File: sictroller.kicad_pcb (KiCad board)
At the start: 6 copper layers, 135.8 x 121.3 mm, 314 parts, among them J1 CONN_01X02, J10 CONN_01X02, J11 RINGTERM, J12 RINGTERM, J14 CONN_01X05, J15 CONN_01X03, J2 CONN_01X08, J3 CONN_02X05, J4 RINGTERM, J5 RINGTERM, J6 RINGTERM, J7 CONN_01X02, J8 RINGTERM, J9 RINGTERM, Q1 CSD17483F4, Q2 CCS050M12CM2, T1 7508110151, U1 ACPL-M61L, U10 74LVC2G04, U11 TXS0108E, U12 MGJ1, U13 MGJ1, U14 2ED020I12-F2, U15 MGJ1, U16 MGJ1, U17 2ED020I12-F2, U18 MGJ1, U19 MGJ1, U2 TMS320F28069M, U20 2ED020I12-F2, U3 ADM3053, U4 TPS76201, U5 TPS76201, U6 XCL221B18, U7 VIPER26HD, U8 ADUM5241, U9 MAX6691, Y1 CSTCE20M0V13C

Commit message: getting there..
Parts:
- added REF**: VIA, sictroller:VIA, F.Cu at (153.4, 124.8)
- added REF**: VIA, sictroller:VIA, F.Cu at (121.7, 133.0)
- moved J15 24.1 mm to (174.4, 128.1)
- moved C16 22.2 mm to (169.9, 105.4)
- moved D1 21.9 mm to (169.4, 102.0)
- moved D2 21.9 mm to (168.4, 105.4)
- moved D3 21.9 mm to (169.5, 98.3)
- moved J2 21.9 mm to (174.4, 102.0)
- moved R2 21.9 mm to (167.7, 103.8)
- moved R3 21.9 mm to (169.6, 103.8)
- moved R4 21.9 mm to (167.5, 101.5)
- moved C22 14.7 mm to (165.8, 131.2)
- moved C18 14.7 mm to (167.2, 131.3)
- moved C19 14.7 mm to (152.8, 129.9)
- moved C24 14.7 mm to (151.5, 127.3)
- moved C25 14.7 mm to (152.8, 127.3)
- moved R10 14.7 mm to (166.2, 122.9)
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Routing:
- net /TI Instaspin MCU/THRUST_PWM: track 0.00 -> 67.0 mm
- net /TI Instaspin MCU/LED1: track 0.00 -> 63.3 mm, vias 0 -> 2
- net /TI Instaspin MCU/LED2: track 0.00 -> 62.8 mm, vias 0 -> 2
- net /TI Instaspin MCU/SW_FLIGHT: track 15.5 -> 72.5 mm, vias 0 -> 3
- net +3V3: track 54.7 -> 96.9 mm, vias 11 -> 15
- net /TI Instaspin MCU/CAN_TX: track 0.00 -> 40.5 mm, vias 0 -> 2
- net /TI Instaspin MCU/CAN_RX: track 0.00 -> 39.8 mm, vias 0 -> 2
- net GND: track 68.8 -> 105.0 mm, vias 41 -> 52
- net +5VD: track 44.3 -> 70.3 mm, vias 11 -> 14
- net /TI Instaspin MCU/TCK: track 0.00 -> 20.1 mm
- net /TI Instaspin MCU/TDO: track 0.00 -> 19.1 mm
- net /TI Instaspin MCU/TDI: track 0.00 -> 17.2 mm
- net /TI Instaspin MCU/GPIO34: track 0.00 -> 16.4 mm, vias 0 -> 2
- net /TI Instaspin MCU/~TRST: track 16.7 -> 30.8 mm, vias 1 -> 2
- net /TI Instaspin MCU/CAN-: track 15.8 -> 8.19 mm
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
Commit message: the end is in sight
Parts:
- added GNDVIA: VIA, sictroller:VIA, F.Cu at (162.0, 52.4)
- added GNDVIA: VIA, sictroller:VIA, F.Cu at (163.3, 49.4)
- added GNDVIA: VIA, sictroller:VIA, F.Cu at (162.3, 50.5)
- added GNDVIA: VIA, sictroller:VIA, F.Cu at (163.3, 52.1)
- added GNDVIA: VIA, sictroller:VIA, F.Cu at (163.1, 48.3)
- added GNDVIA: VIA, sictroller:VIA, F.Cu at (162.3, 48.3)
- added R50: 100K, Resistors_SMD:R_0402, F.Cu at (170.5, 80.4)
- C123: moved to F.Cu
- Q1: footprint sictroller:FEMTOFET_YJC_YJJ -> FEMTOFET_YJC_YJJ
- moved C55 9.44 mm to (166.1, 77.3), turned to 90 degrees
- moved R18 8.45 mm to (154.2, 52.1)
- moved L1 8.38 mm to (156.8, 52.1)
- moved C52 8.00 mm to (169.3, 68.5), turned to 270 degrees
- moved D7 7.00 mm to (169.3, 70.6)
- moved R42 6.89 mm to (167.7, 69.2)
- moved C53 6.76 mm to (166.9, 70.9), turned to 180 degrees
- moved Q1 4.40 mm to (173.0, 78.0), turned to 180 degrees
- moved R48 3.91 mm to (165.8, 61.8), turned to 0 degrees
- moved R43 3.52 mm to (170.1, 81.9), turned to 270 degrees
- moved U8 1.98 mm to (169.4, 75.2)
- moved C56 1.85 mm to (170.6, 79.4)
- moved R45 1.82 mm to (172.9, 76.6), turned to 180 degrees
- moved C123 1.74 mm to (132.8, 113.6), turned to 90 degrees
- moved W23 1.03 mm to (166.6, 60.4)
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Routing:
- net /Feedback/TEMP_PWM: track 0.00 -> 75.4 mm
- net /Feedback/TEMP_EN: track 0.00 -> 73.2 mm
- net CCS_NTC_2: track 0.00 -> 56.8 mm, vias 0 -> 6
- net /TI Instaspin MCU/SW_BRAKE: track 13.5 -> 67.3 mm, vias 0 -> 2
- net /TI Instaspin MCU/SW_EMERG: track 17.8 -> 70.9 mm, vias 0 -> 2
- net CCS_NTC_1: track 0.00 -> 47.1 mm
- net GND: track 105.0 -> 138.7 mm, vias 52 -> 66
- net Net-(R22-Pad2): track 0.00 -> 28.9 mm, vias 0 -> 1
- net +5VD: track 70.3 -> 97.3 mm, vias 14 -> 22
- net /LV power supplies/HV: track 0.00 -> 26.7 mm, vias 0 -> 1
- net /TI Instaspin MCU/TMS: track 0.00 -> 21.0 mm, vias 0 -> 2
- net Net-(D8-Pad2): track 0.00 -> 13.7 mm
- net BUS+: track 14.4 -> 25.3 mm
- net Net-(D8-Pad1): track 0.00 -> 8.46 mm
- net /LV power supplies/VIPER_VDD: track 0.00 -> 7.61 mm, vias 0 -> 1
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- added copper zone on B.Cu, net /LV power supplies/SW
- added copper zone on In1.Cu, net CCS_NTC_2

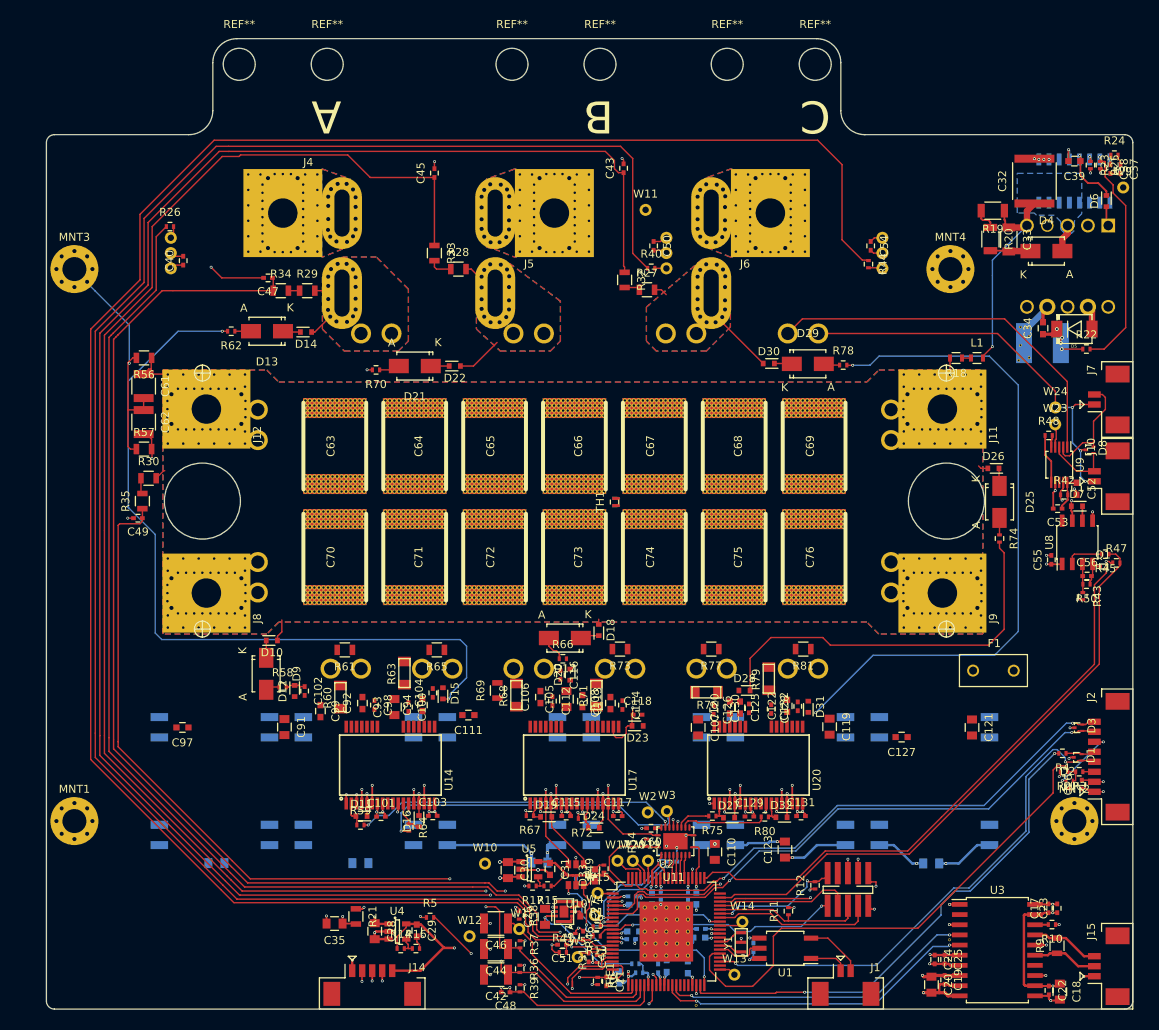
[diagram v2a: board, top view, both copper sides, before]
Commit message: 0 not connected
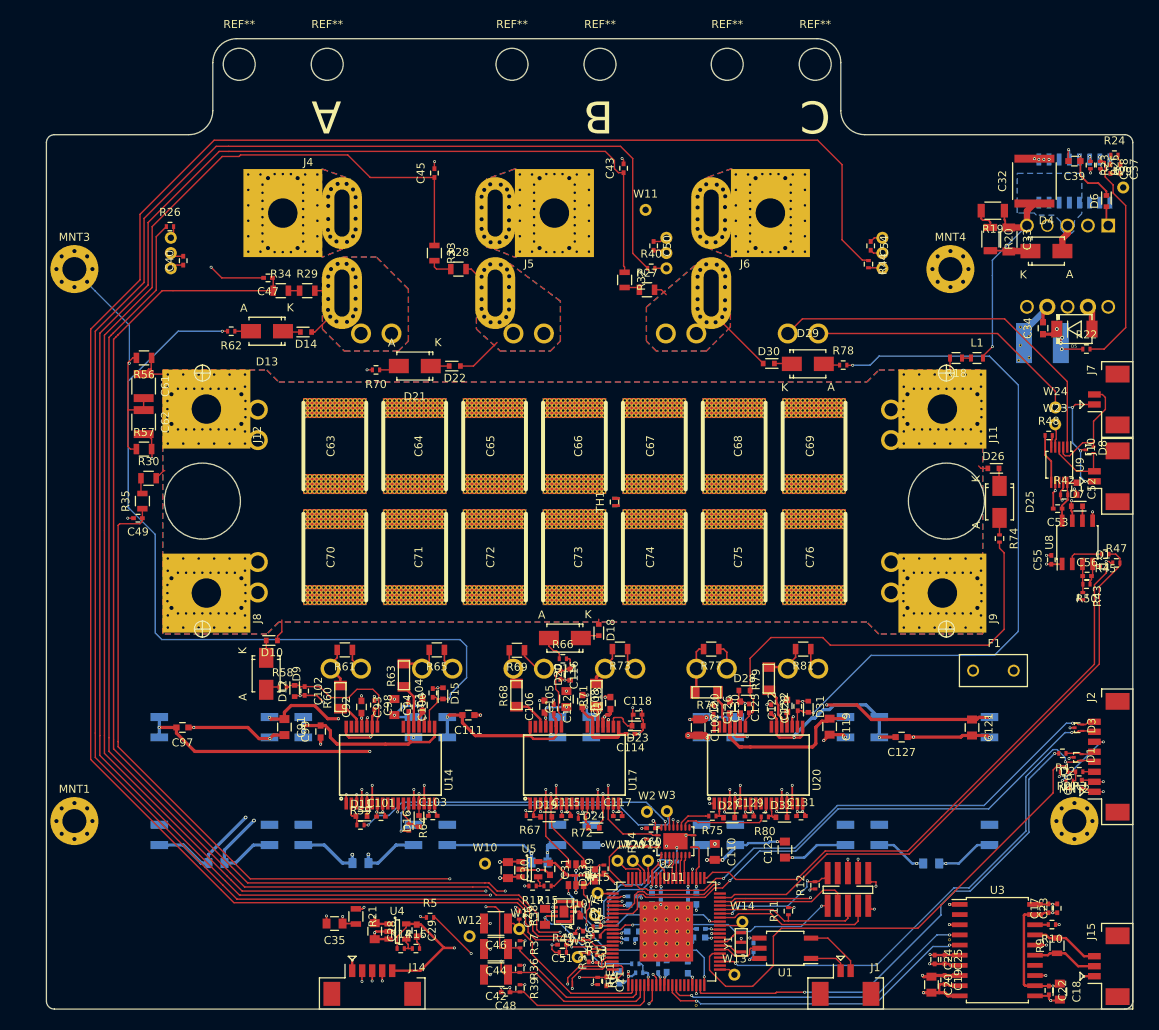
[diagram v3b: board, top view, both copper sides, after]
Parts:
- moved R69 5.59 mm to (99.3, 88.6), turned to 180 degrees
- moved C114 3.75 mm to (113.5, 99.1), turned to 180 degrees
- moved C99 2.56 mm to (74.8, 98.8), turned to 90 degrees
- moved C106 1.29 mm to (102.8, 95.7)
- moved C112 1.00 mm to (103.9, 96.0)
- moved C92 0.50 mm to (79.9, 95.7)
- moved R63 0.28 mm to (85.2, 91.8)
- moved W2 0.13 mm to (115.6, 108.8)
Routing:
- net /Power stage/Halfbridge Driver A/SRC_H: track 0.00 -> 40.4 mm, vias 0 -> 7
- net /Power stage/Halfbridge Driver A/-5V_HS: track 0.00 -> 40.3 mm, vias 0 -> 3
- net /Power stage/Halfbridge Driver C/SRC_L: track 0.00 -> 33.4 mm, vias 0 -> 6
- net GND: track 138.7 -> 169.8 mm, vias 66 -> 72
- net /Power stage/Halfbridge Driver C/+19V_LS: track 0.00 -> 28.4 mm, vias 0 -> 3
- net /Power stage/Halfbridge Driver A/-5V_LS: track 0.00 -> 26.1 mm, vias 0 -> 1
- net /Power stage/Halfbridge Driver C/-5V_LS: track 0.00 -> 25.2 mm, vias 0 -> 2
- net /Power stage/Halfbridge Driver C/SRC_H: track 0.00 -> 24.7 mm, vias 0 -> 6
- net +5VD: track 97.3 -> 120.0 mm, vias 22 -> 25
- net /Power stage/Halfbridge Driver B/-5V_HS: track 0.00 -> 22.3 mm, vias 0 -> 1
- net /Power stage/Halfbridge Driver C/+19V_HS: track 0.00 -> 20.7 mm, vias 0 -> 1
- net /Power stage/Halfbridge Driver B/SRC_L: track 0.00 -> 18.0 mm, vias 0 -> 7
- net /Power stage/Halfbridge Driver B/+19V_LS: track 0.00 -> 16.6 mm, vias 0 -> 3
- net /Power stage/Halfbridge Driver A/+19V_HS: track 0.00 -> 16.0 mm, vias 0 -> 3
- net /Power stage/Halfbridge Driver A/SRC_L: track 0.00 -> 15.9 mm, vias 0 -> 7
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
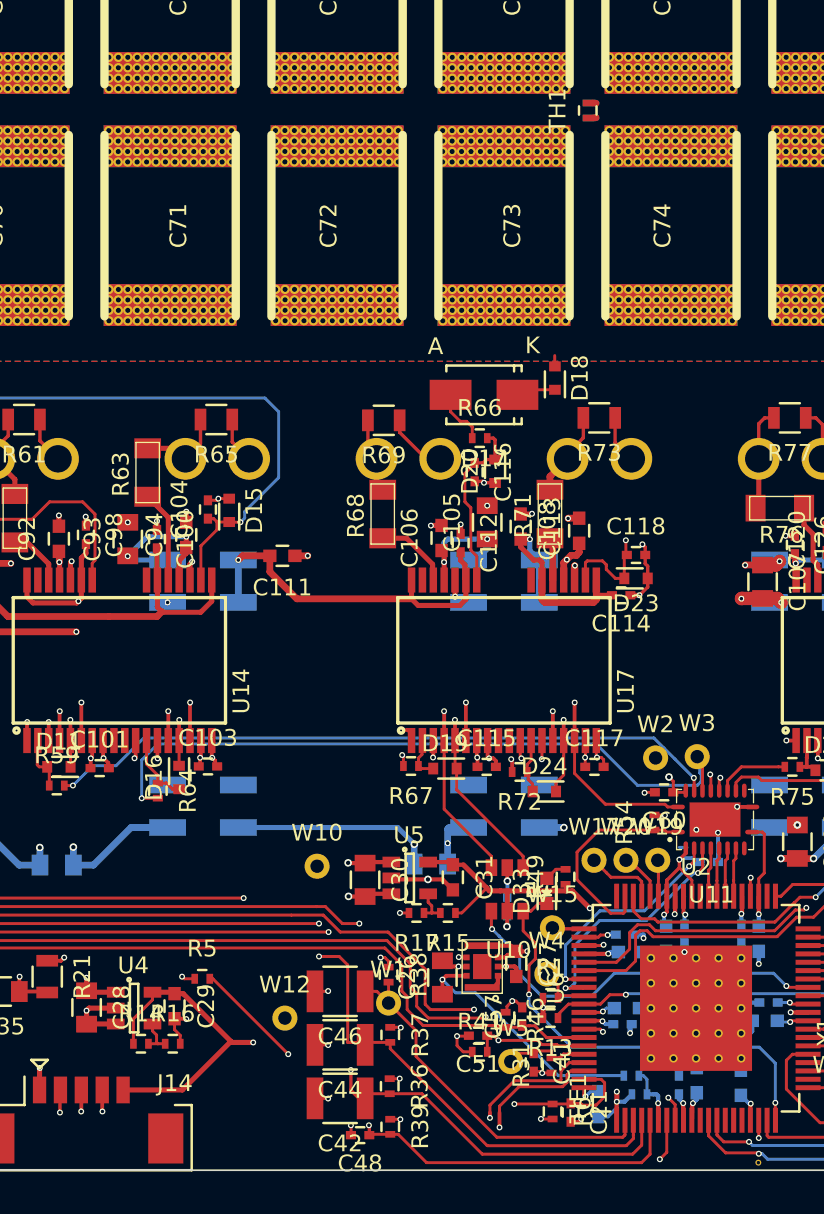
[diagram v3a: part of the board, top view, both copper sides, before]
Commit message: DRC pass (haven't checked 9/9 on inner layers)
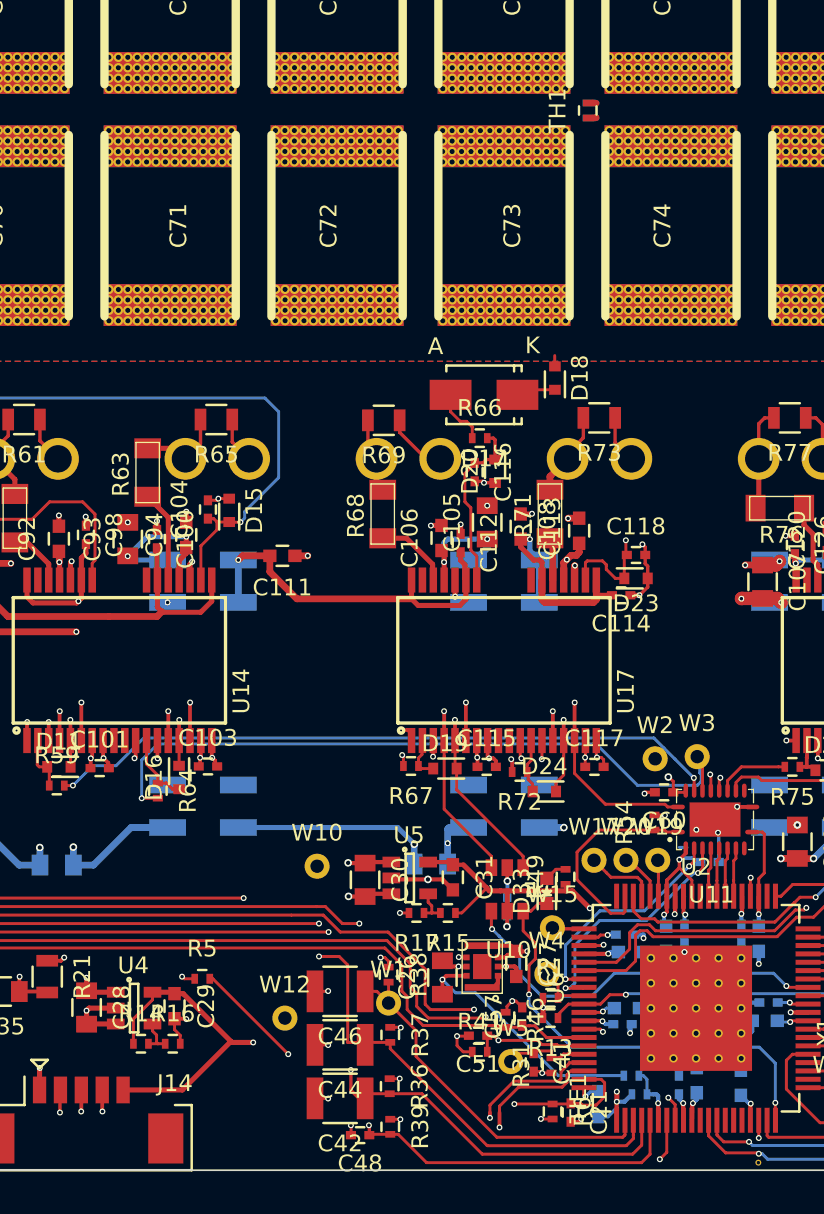
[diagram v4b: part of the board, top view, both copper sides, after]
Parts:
- moved W2 0.06 mm to (115.5, 108.9)

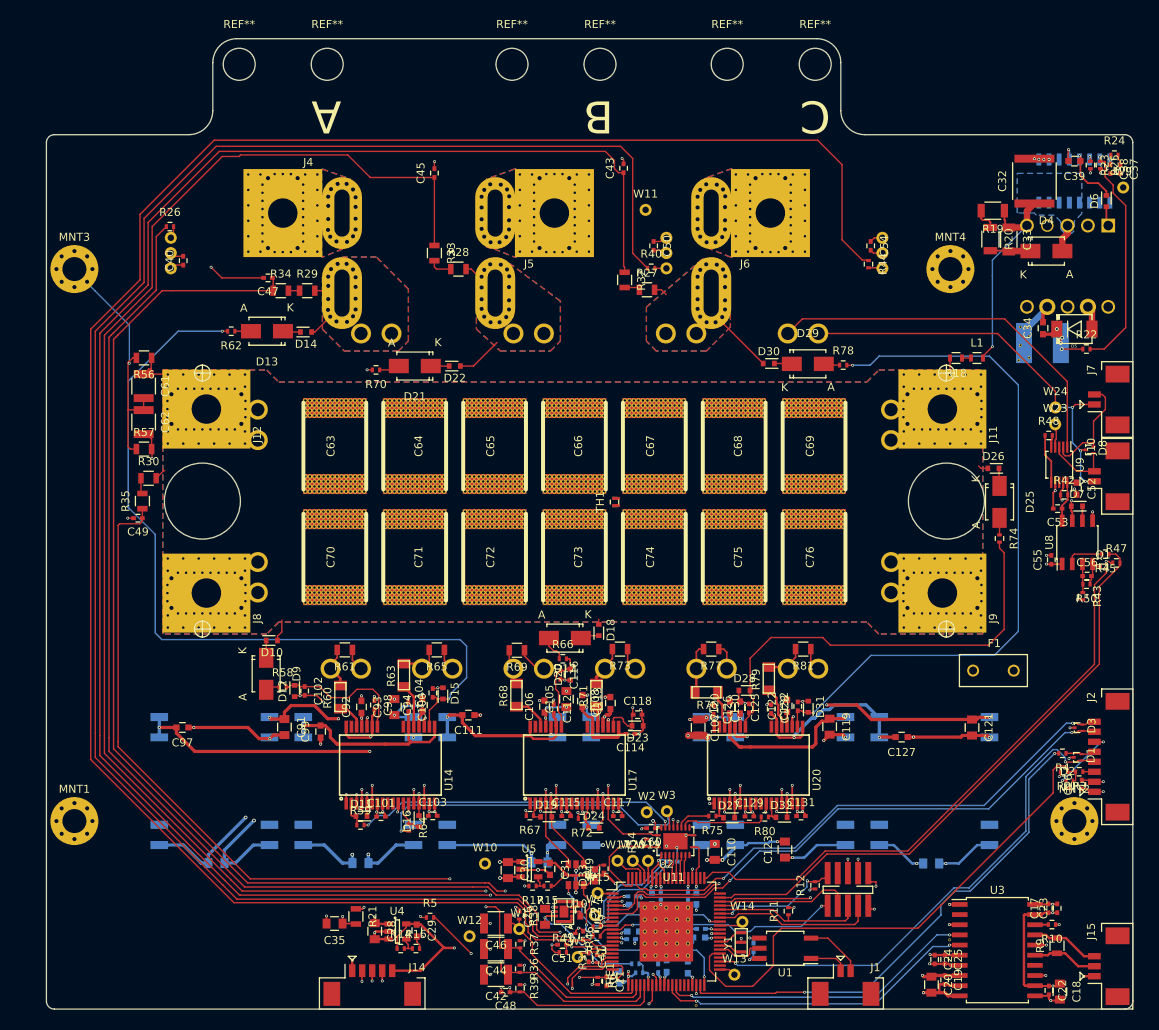
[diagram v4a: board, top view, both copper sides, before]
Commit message: inner layer 9/9 visually checked; starting silkscreen
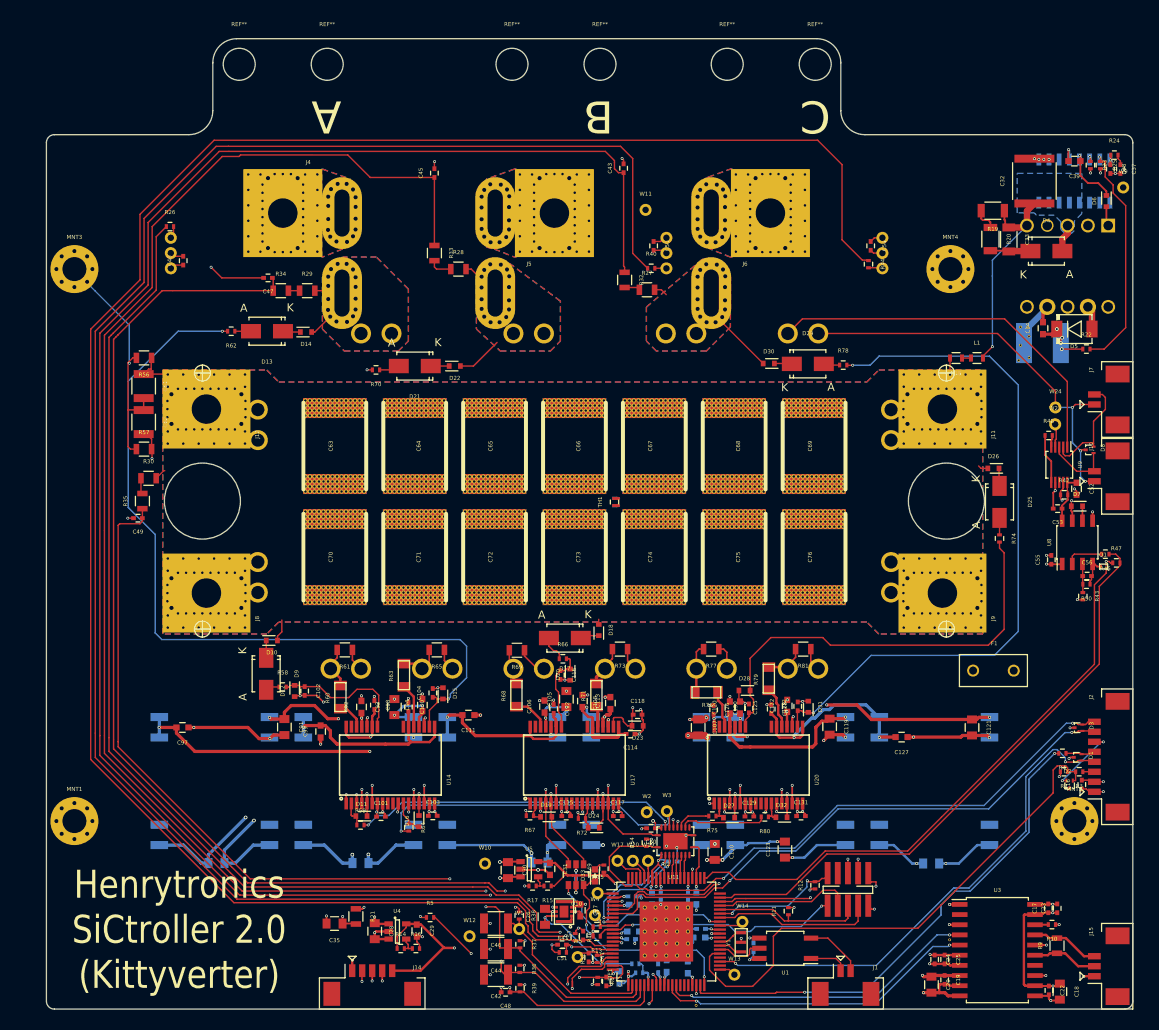
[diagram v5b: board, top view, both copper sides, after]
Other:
- board text added: "Henrytronics SiCtroller 2.0 (Kittyverter)"

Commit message: silkscreen progress
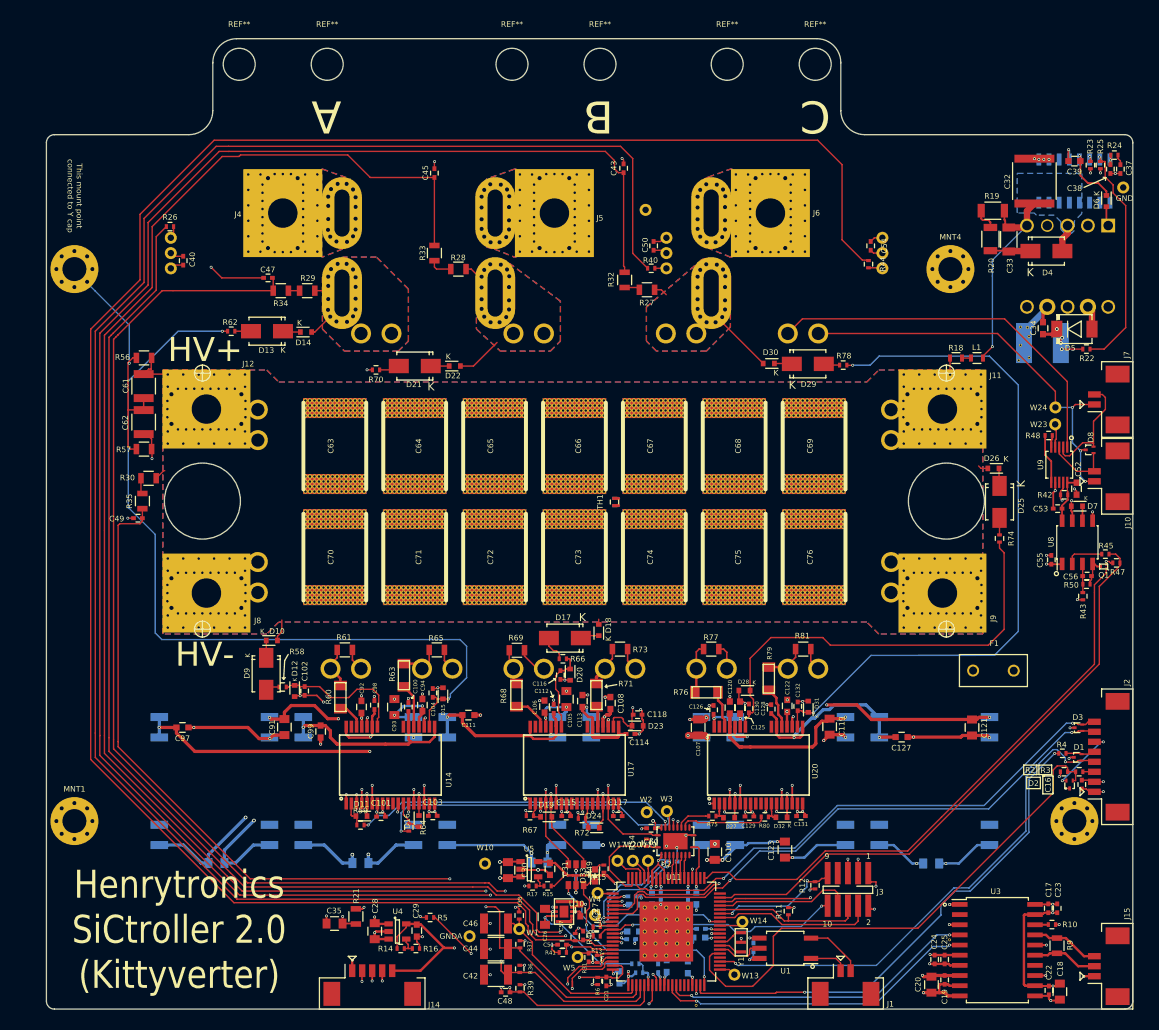
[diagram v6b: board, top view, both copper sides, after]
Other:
- board text added: "1"
- board text added: "10"
- board text added: "2"
- board text added: "9"
- board text added: "GND"
- board text added: "GNDA"
- board text added: "HV+"
- board text added: "HV-"
- board text added: "J3"
- board text added: "K"
- board text added: "This mount point connected to Y cap"

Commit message: silkscreen complete top side?
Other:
- board text added: "Serial:"
